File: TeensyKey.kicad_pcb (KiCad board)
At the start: 2 copper layers, 3 parts, among them SW1 MX-with-LED, U1 Teensy3.2

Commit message: added board edge
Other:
- board outline added: 35.2 x 35.2 mm
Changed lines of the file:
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@@
   (general
     (thickness 1.6)
-    (drawings 0)
+    (drawings 1)
     (tracks 0)
     (zones 0)
@@
       (net 5 "Net-(SW1-Pad4)"))
   )
+  (gr_circle (center 142.85 77.33) (end 158.98 70.32) (layer Edge.Cuts) (width 0.05))
 )

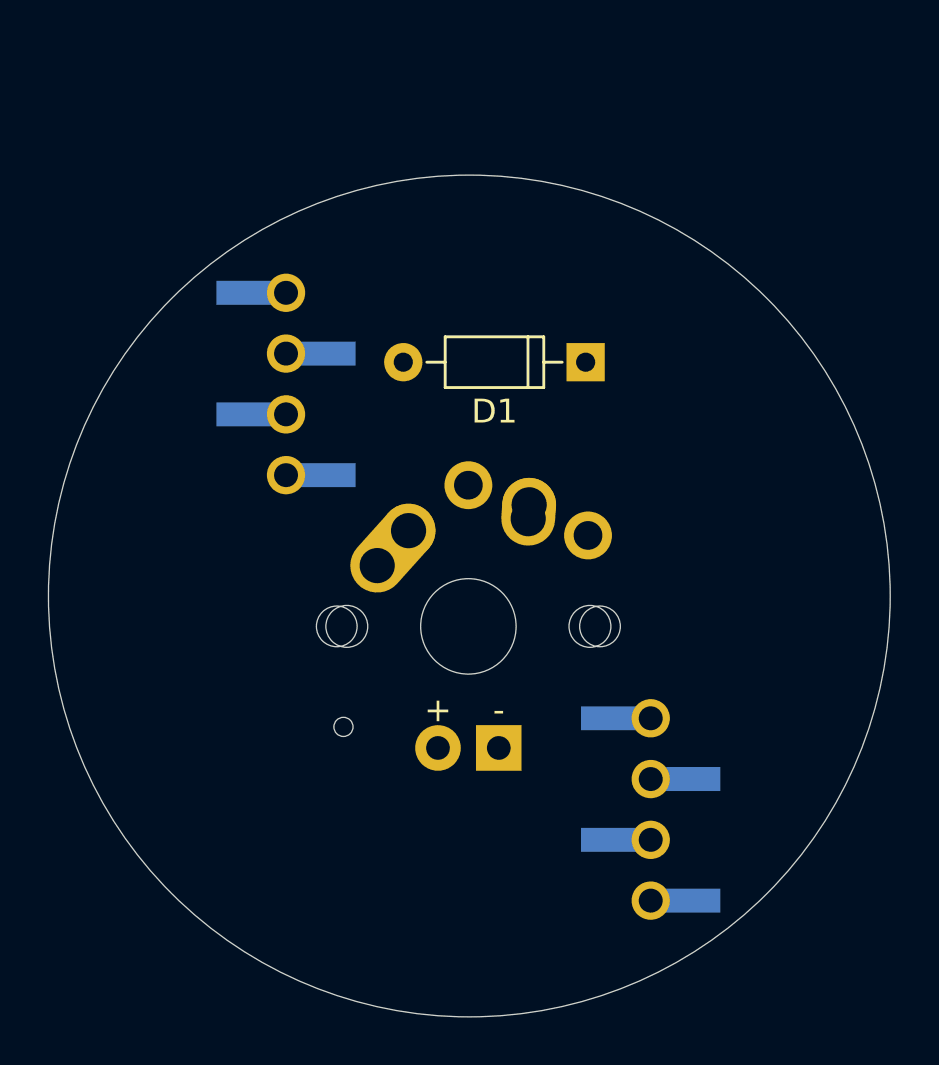
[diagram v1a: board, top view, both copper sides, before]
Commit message: routed traces
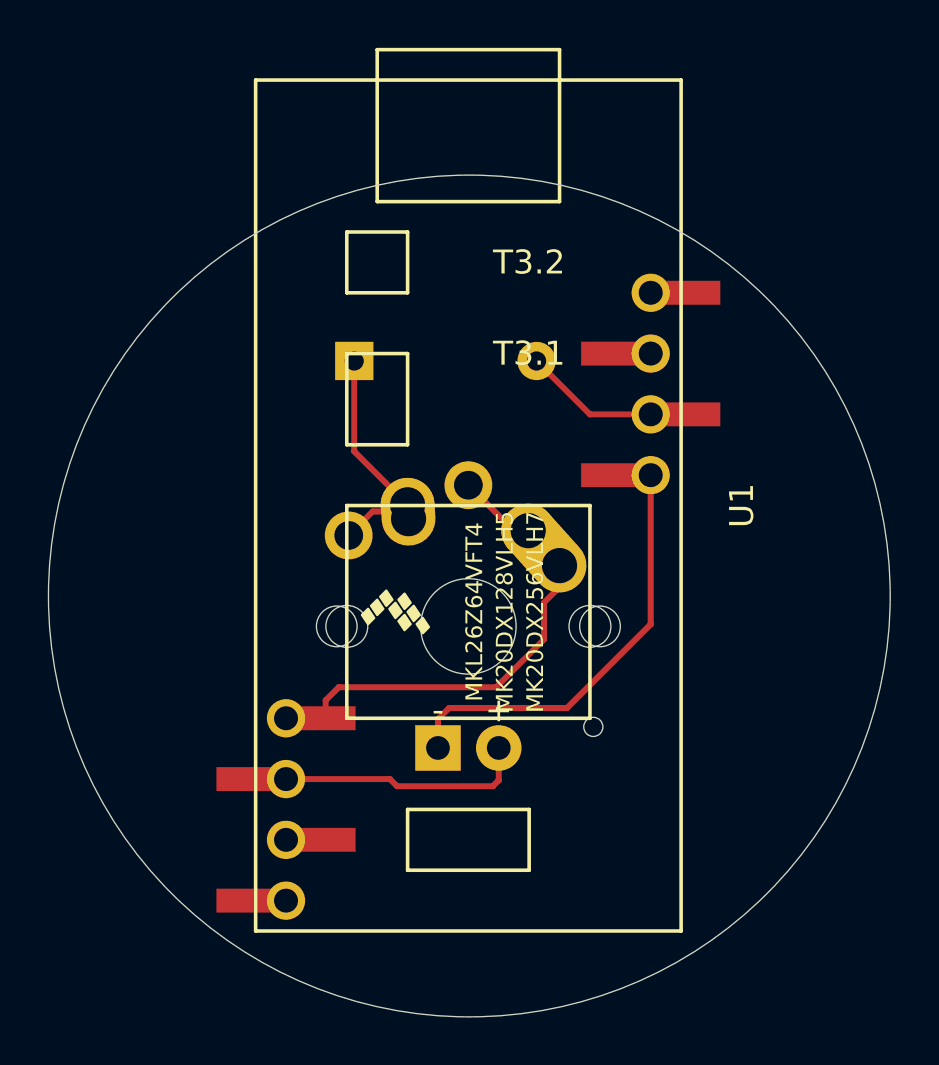
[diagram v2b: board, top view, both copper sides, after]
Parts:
- D1, SW1: moved to B.Cu
- U1: moved to F.Cu
- moved D1 9.67 mm to (138.0, 67.5), turned to 0 degrees
- turned SW1 to 180 degrees
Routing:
- net Net-(SW1-Pad1): track 0.00 -> 19.5 mm
- net Net-(SW1-Pad4): track 0.00 -> 18.0 mm
- net Net-(SW1-Pad3): track 0.00 -> 10.5 mm
- net Net-(D1-Pad1): track 0.00 -> 9.92 mm
- net Net-(D1-Pad2): track 0.00 -> 5.69 mm

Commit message: added mounting holes
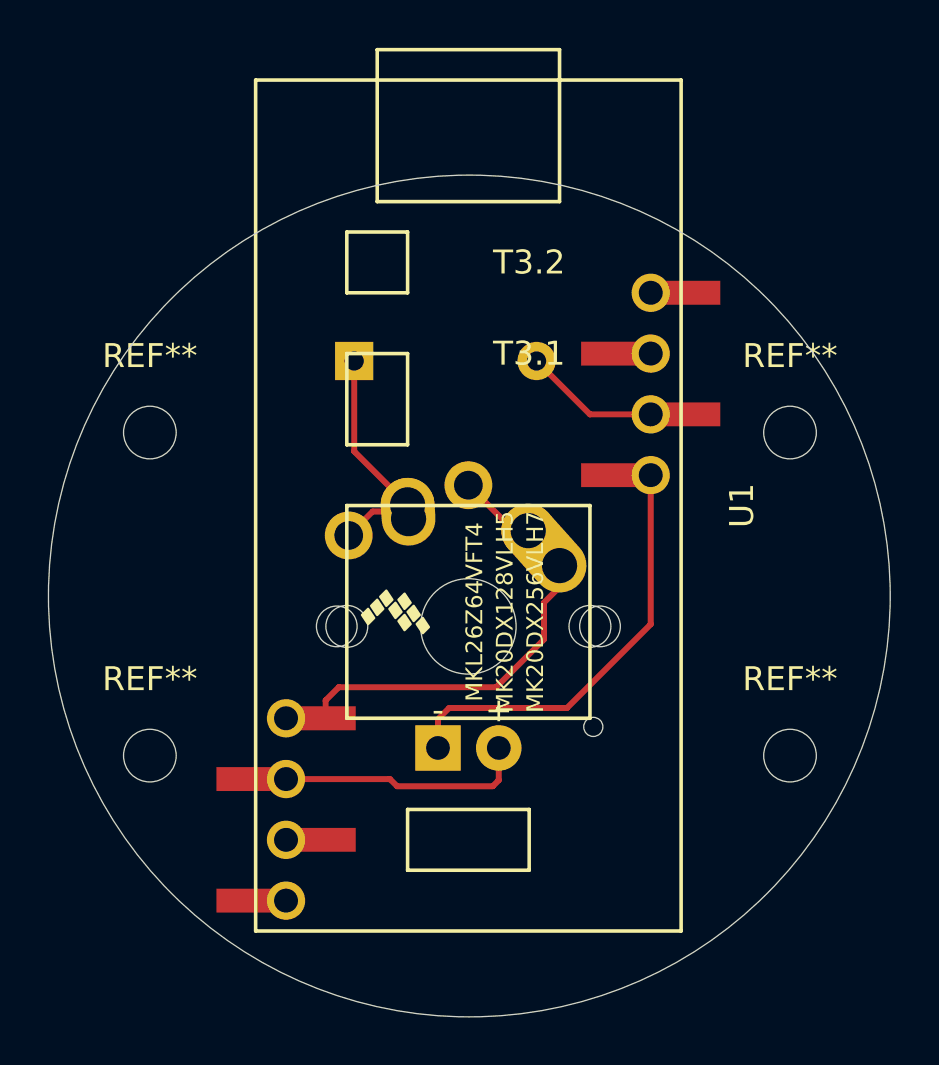
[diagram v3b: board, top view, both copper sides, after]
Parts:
- added REF**: MountingHole_2.2mm_M2, Mounting_Holes:MountingHole_2.2mm_M2, F.Cu at (156.2, 84.0)
- added REF**: MountingHole_2.2mm_M2, Mounting_Holes:MountingHole_2.2mm_M2, F.Cu at (156.2, 70.5)
- added REF**: MountingHole_2.2mm_M2, Mounting_Holes:MountingHole_2.2mm_M2, F.Cu at (129.5, 84.0)
- added REF**: MountingHole_2.2mm_M2, Mounting_Holes:MountingHole_2.2mm_M2, F.Cu at (129.5, 70.5)
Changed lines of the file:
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@@
     (tracks 26)
     (zones 0)
-    (modules 3)
+    (modules 7)
     (nets 30)
   )
@@
     (add_net "Net-(U1-Pad9)")
   )
+  (module Mounting_Holes:MountingHole_2.2mm_M2 (layer F.Cu)
+    (at 156.25 84)
+    (descr "Mounting Hole 2.2mm, no annular, M2")
+    (tags "mounting hole 2.2mm no annular m2")
+    (attr virtual)
+    (fp_text reference REF** (at 0 -3.2) (layer F.SilkS)
+      (effects (font (size 1 1) (thickness 0.15)))
+    )
+    (fp_text value MountingHole_2.2mm_M2 (at 0 3.2) (layer F.Fab)
+      (effects (font (size 1 1) (thickness 0.15)))
+    )
+    (fp_text user %R (at 0.3 0) (layer F.Fab)
+      (effects (font (size 1 1) (thickness 0.15)))
+    )
+    (fp_circle (center 0 0) (end 2.2 0) (layer Cmts.User) (width 0.15))
+    (fp_circle (center 0 0) (end 2.45 0) (layer F.CrtYd) (width 0.05))
+    (pad 1 np_thru_hole circle (at 0 0) (size 2.2 2.2) (drill 2.2) (layers *.Cu *.Mask))
+  )
+  (module Mounting_Holes:MountingHole_2.2mm_M2 (layer F.Cu)
+    (at 156.25 70.5)
+    (descr "Mounting Hole 2.2mm, no annular, M2")
+    (tags "mounting hole 2.2mm no annular m2")
+    (attr virtual)
+    (fp_text reference REF** (at 0 -3.2) (layer F.SilkS)
+      (effects (font (size 1 1) (thickness 0.15)))
+    )
+    (fp_text value MountingHole_2.2mm_M2 (at 0 3.2) (layer F.Fab)
+      (effects (font (size 1 1) (thickness 0.15)))
+    )
+    (fp_text user %R (at 0.3 0) (layer F.Fab)
+      (effects (font (size 1 1) (thickness 0.15)))
+    )
+    (fp_circle (center 0 0) (end 2.2 0) (layer Cmts.User) (width 0.15))
+    (fp_circle (center 0 0) (end 2.45 0) (layer F.CrtYd) (width 0.05))
+    (pad 1 np_thru_hole circle (at 0 0) (size 2.2 2.2) (drill 2.2) (layers *.Cu *.Mask))
+  )
+  (module Mounting_Holes:MountingHole_2.2mm_M2 (layer F.Cu)
+    (at 129.5 84)
+    (descr "Mounting Hole 2.2mm, no annular, M2")
+    (tags "mounting hole 2.2mm no annular m2")
+    (attr virtual)
+    (fp_text reference REF** (at 0 -3.2) (layer F.SilkS)
+      (effects (font (size 1 1) (thickness 0.15)))
+    )
+    (fp_text value MountingHole_2.2mm_M2 (at 0 3.2) (layer F.Fab)
+      (effects (font (size 1 1) (thickness 0.15)))
+    )
+    (fp_text user %R (at 0.3 0) (layer F.Fab)
+      (effects (font (size 1 1) (thickness 0.15)))
+    )
+    (fp_circle (center 0 0) (end 2.2 0) (layer Cmts.User) (width 0.15))
+    (fp_circle (center 0 0) (end 2.45 0) (layer F.CrtYd) (width 0.05))
+    (pad 1 np_thru_hole circle (at 0 0) (size 2.2 2.2) (drill 2.2) (layers *.Cu *.Mask))
+  )
+  (module Mounting_Holes:MountingHole_2.2mm_M2 (layer F.Cu)
+    (at 129.5 70.5)
+    (descr "Mounting Hole 2.2mm, no annular, M2")
+    (tags "mounting hole 2.2mm no annular m2")
+    (attr virtual)
+    (fp_text reference REF** (at 0 -3.2) (layer F.SilkS)
+      (effects (font (size 1 1) (thickness 0.15)))
+    )
+    (fp_text value MountingHole_2.2mm_M2 (at 0 3.2) (layer F.Fab)
+      (effects (font (size 1 1) (thickness 0.15)))
+    )
+    (fp_text user %R (at 0.3 0) (layer F.Fab)
+      (effects (font (size 1 1) (thickness 0.15)))
+    )
+    (fp_circle (center 0 0) (end 2.2 0) (layer Cmts.User) (width 0.15))
+    (fp_circle (center 0 0) (end 2.45 0) (layer F.CrtYd) (width 0.05))
+    (pad 1 np_thru_hole circle (at 0 0) (size 2.2 2.2) (drill 2.2) (layers *.Cu *.Mask))
+  )
   (module chillpizza:Teensy30_31_32_LC_smt_combi (layer F.Cu)
